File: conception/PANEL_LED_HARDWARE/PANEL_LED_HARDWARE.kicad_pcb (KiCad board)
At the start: 2 copper layers, 62.2 x 50.8 mm, 27 parts, among them J1 PWR, J2 PWR_TO_LED, J3 PWR_TO_LED, J4 Connector to pannel led, J5 EXT PIN, U1 LMR51430, U2 LMR51430, U3 74HC374

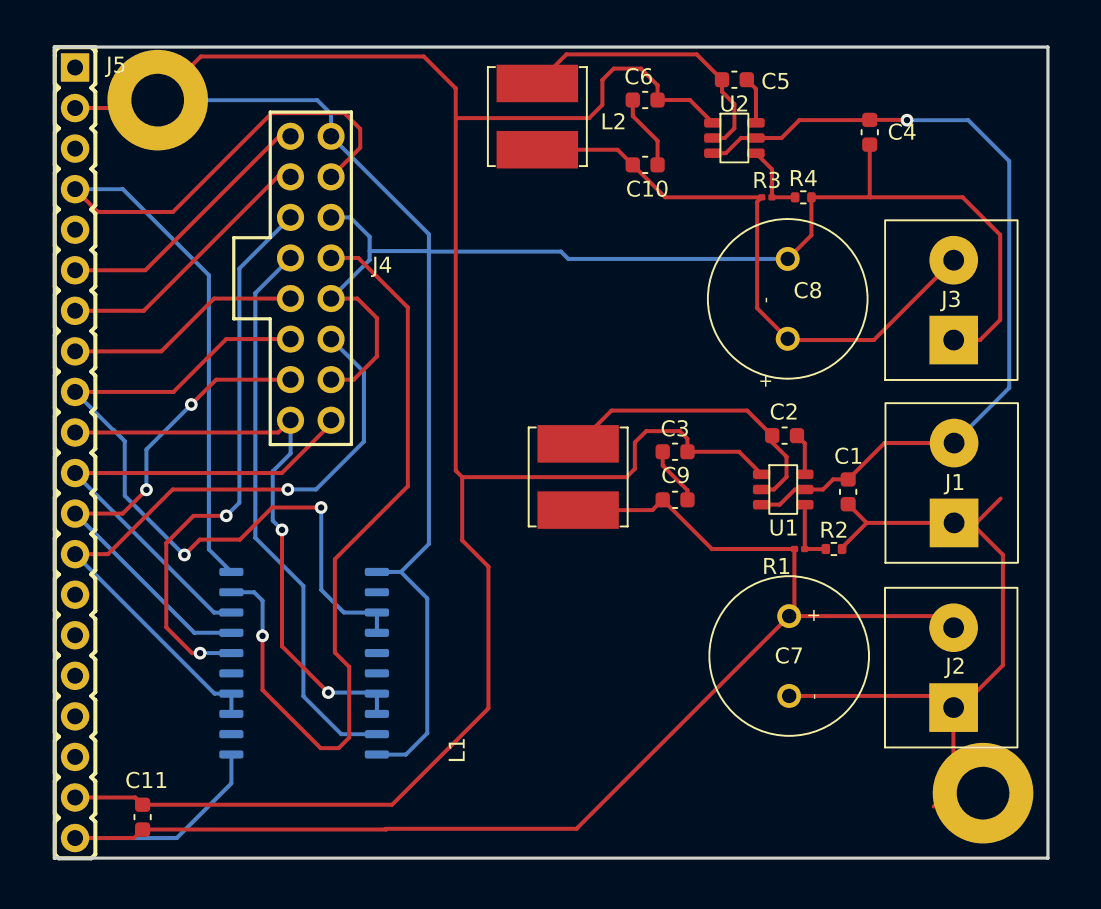
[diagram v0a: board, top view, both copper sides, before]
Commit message: Update PCB routage
Increase pistes width for 24V 5V and GND
Change power supply for buffer 5V=>3.3V
Add GND and other signal plan like the example in the datasheet (LMR51430)
Move connectors
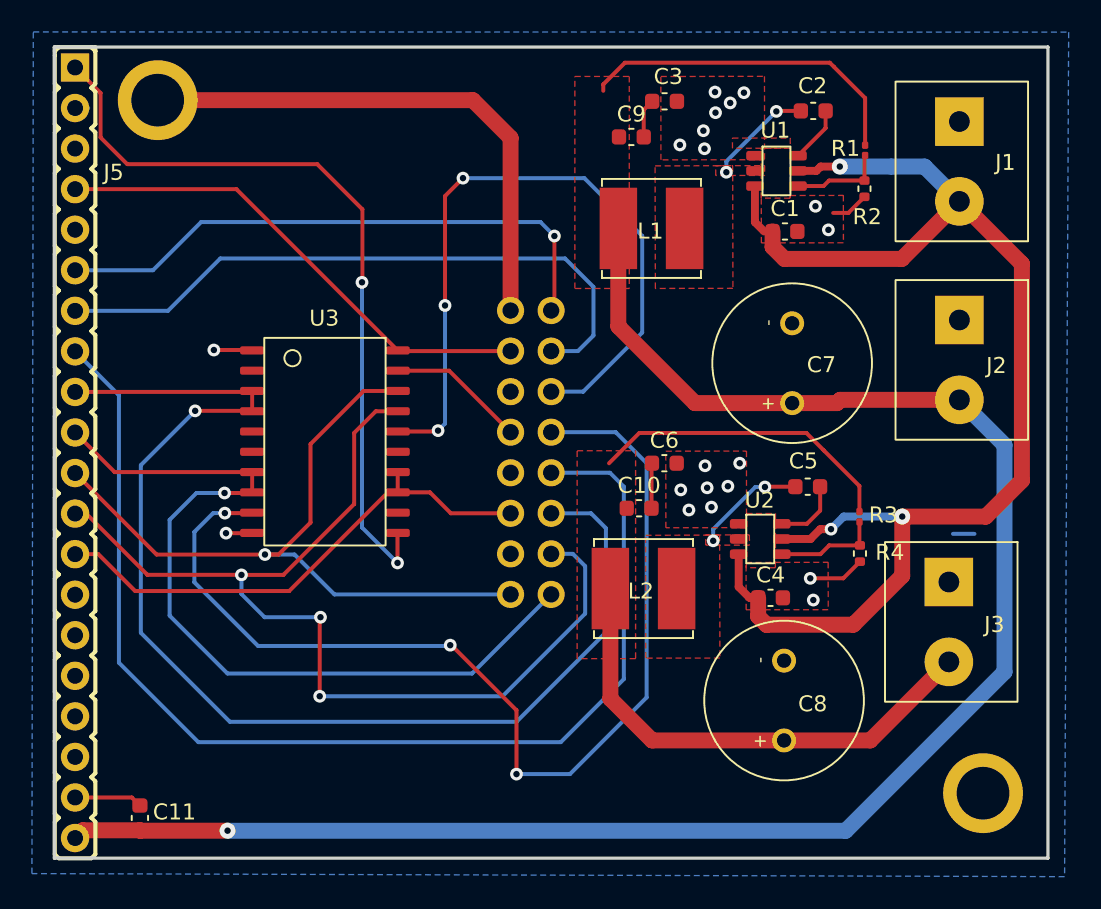
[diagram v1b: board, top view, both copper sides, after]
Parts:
- J4: moved to B.Cu
- U3: moved to F.Cu
- moved J1 31.4 mm to (147.6, 48.1), turned to -90 degrees
- moved J2 30.6 mm to (147.6, 60.5), turned to -90 degrees
- moved L2 30.3 mm to (123.5, 79.9), turned to 180 degrees
- moved C4 29.8 mm to (131.5, 80.4), turned to 0 degrees
- moved C5 25.9 mm to (133.8, 73.5)
- moved R1 25.3 mm to (137.4, 52.4), turned to -90 degrees
- moved U2 25.2 mm to (130.0, 75.2)
- moved C8 25.2 mm to (132.3, 86.9)
- moved C9 22.9 mm to (122.8, 51.6)
- moved C6 22.8 mm to (124.8, 72.0)
- moved R2 22.6 mm to (137.4, 54.8), turned to -90 degrees
- moved R4 22.6 mm to (137.1, 77.7), turned to -90 degrees
- moved C3 22.0 mm to (124.8, 49.3)
- moved C10 21.5 mm to (123.3, 74.8)
- moved R3 20.8 mm to (137.1, 75.4), turned to -90 degrees
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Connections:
- U3 pad 20: +5V -> +3V3
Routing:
- net GND: track 316.8 -> 51.2 mm, vias 0 -> 20
- net /GPIO13\PANEL_B2: track 14.9 -> 72.9 mm
- net +3V3: track 0.38 -> 48.6 mm, vias 0 -> 2
- net /PANEL_B: track 50.3 -> 8.67 mm, vias 1 -> 0
- net +5V: track 93.9 -> 131.8 mm, vias 0 -> 1
- net /GPIO17\PANEL_B1: track 31.3 -> 64.6 mm, vias 2 -> 3
- net /PANEL_A: track 35.2 -> 66.4 mm, vias 0 -> 3
- net /Vin +24V: track 53.2 -> 83.8 mm, vias 1 -> 3
- net /GPIO14\PANEL_R2: track 48.2 -> 75.4 mm, vias 2 -> 1
- net /GPI012\PANEL_CLK: track 17.0 -> 40.7 mm
- net /GPIO5\PANEL_LAT: track 55.0 -> 31.5 mm
- net /GPI04\PANEL_OE: track 17.0 -> 36.4 mm, vias 0 -> 1
- net /GPI015\PANEL_R1: track 37.1 -> 52.7 mm, vias 2 -> 1
- net /GPIO16\PANEL_G1: track 31.0 -> 45.9 mm, vias 0 -> 1
- net /+5V Regu 2: track 38.1 -> 50.7 mm
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- added copper zone on F.Cu, net +5V
- added copper zone on F.Cu, net /+5V Regu 2
- added copper zone on F.Cu, net /Vout
- added copper zone on F.Cu, net /Vout2
- added copper zone on B.Cu, net GND
- added copper zone on F.Cu, net GND

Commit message: Review PCB
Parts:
- R2, R4: footprint Resistor_SMD:R_0402_1005Metric -> Resistor_SMD:R_0201_0603Metric
- moved C3 23.6 mm to (123.2, 72.8)
- moved C6 22.2 mm to (122.8, 49.9)
- moved R1 1.72 mm to (137.3, 50.7)
- moved C4 1.24 mm to (130.2, 80.5)
- moved C1 1.12 mm to (131.3, 57.5)
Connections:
- C10 pad 2: Net-(C10-Pad2) -> GND
- C3 pad 1: Net-(C3-Pad1) -> /+5V Regu 2
- C6 pad 1: Net-(C10-Pad2) -> +5V
- C9 pad 2: Net-(C3-Pad1) -> GND
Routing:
- net /PANEL_A: track 66.4 -> 22.0 mm, vias 3 -> 2
- net /GPIO13\PANEL_B2: track 72.9 -> 34.2 mm, vias 0 -> 1
- net /GPIO14\PANEL_R2: track 75.4 -> 38.3 mm, vias 1 -> 2
- net /PANEL_C: track 45.1 -> 10.6 mm, vias 3 -> 1
- net GND: track 51.2 -> 21.4 mm, vias 20 -> 18
- net /GPIO17\PANEL_B1: track 64.6 -> 41.9 mm, vias 3 -> 2
- net /GPI015\PANEL_R1: track 52.7 -> 37.0 mm, vias 1 -> 2
- net /GPI012\PANEL_CLK: track 40.7 -> 31.1 mm, vias 0 -> 2
- net /+5V Regu 2: track 50.7 -> 58.0 mm
- net +5V: track 131.8 -> 137.8 mm
- net /GPI04\PANEL_OE: track 36.4 -> 31.2 mm, vias 1 -> 2
- net /GPIO5\PANEL_LAT: track 31.5 -> 35.7 mm
- net /FB: track 5.89 -> 9.07 mm
- net Net-(C10-Pad2): track 2.83 -> 0.00 mm
- net Net-(C3-Pad1): track 2.45 -> 0.00 mm
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- removed copper zone on F.Cu, net +5V
- removed copper zone on F.Cu, net /+5V Regu 2

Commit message: test com buffer
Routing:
- net /Vout: track 6.65 -> 2.23 mm
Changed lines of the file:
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@@
       (net 2 "GND") (pintype "passive"))
   )
+  (gr_circle (center 130.45 51.8) (end 130.65 51.8) (layer "F.SilkS") (width 0.15) (fill solid))
+  (gr_circle (center 129.4 74.9) (end 129.6 74.9) (layer "F.SilkS") (width 0.15) (fill solid))
   (gr_rect (start 86.63 45.94) (end 148.86 96.74) (layer "Edge.Cuts") (width 0.2) (fill none))
   (segment (start 139.92 59) (end 143.315 55.605) (width 0.5) (layer "F.Cu") (net 1))
@@
   (via (at 128.72 53.78) (size 0.8) (drill 0.4) (layers "F.Cu" "B.Cu") (net 26))
   (segment (start 128.72 53.78) (end 128.72 53.1) (width 0.25) (layer "B.Cu") (net 26))
-  (segment (start 128.72 53.1) (end 131.85 49.97) (width 0.25) (layer "B.Cu") (net 26))
   (segment (start 131.155 73.475) (end 131.135 73.495) (width 0.25) (layer "F.Cu") (net 27))
   (segment (start 133.04 73.475) (end 131.155 73.475) (width 0.25) (layer "F.Cu") (net 27))
@@
     (connect_pads (clearance 0))
     (min_thickness 0.254)
-    (keepout (tracks allowed) (vias allowed) (pads allowed ) (copperpour not_allowed) (footprints allowed))
+    (keepout (tracks allowed) (vias allowed) (pads allowed) (copperpour not_allowed) (footprints allowed))
     (fill (thermal_gap 0.508) (thermal_bridge_width 0.508))
     (polygon
